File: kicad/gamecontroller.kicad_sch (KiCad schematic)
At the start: 19 parts, among them SW1 SW_Push, SW2 SW_Push, SW3 SW_Push, SW4 SW_Push, SW5 SW_Push, SW6 SW_Push

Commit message: Updates to kicad files and update espinput submodule
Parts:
- removed U1: ~, ESP32_30pin:ESP32_30pin, symbol esp32_30pin:ESP32_30Pin
- added COM-09302: COM-09032, COM_09032:COM_09032, symbol COM-09032:COM-09032
- added D1: LED, LED_THT:LED_D3.0mm, symbol Device:LED
- added ESP32: ESP32_30pin, ESP32_30pin:ESP32_30pin, symbol ESP32_30pin:ESP32_30Pin
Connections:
- net +3.3V: now also COM-09302.H1 (H+), COM-09302.V1 (V+)
- net GND: now also COM-09302.B2A (SEL-), COM-09302.H3 (H-), COM-09302.V3 (V-)
- no-connect marks 24 -> 28

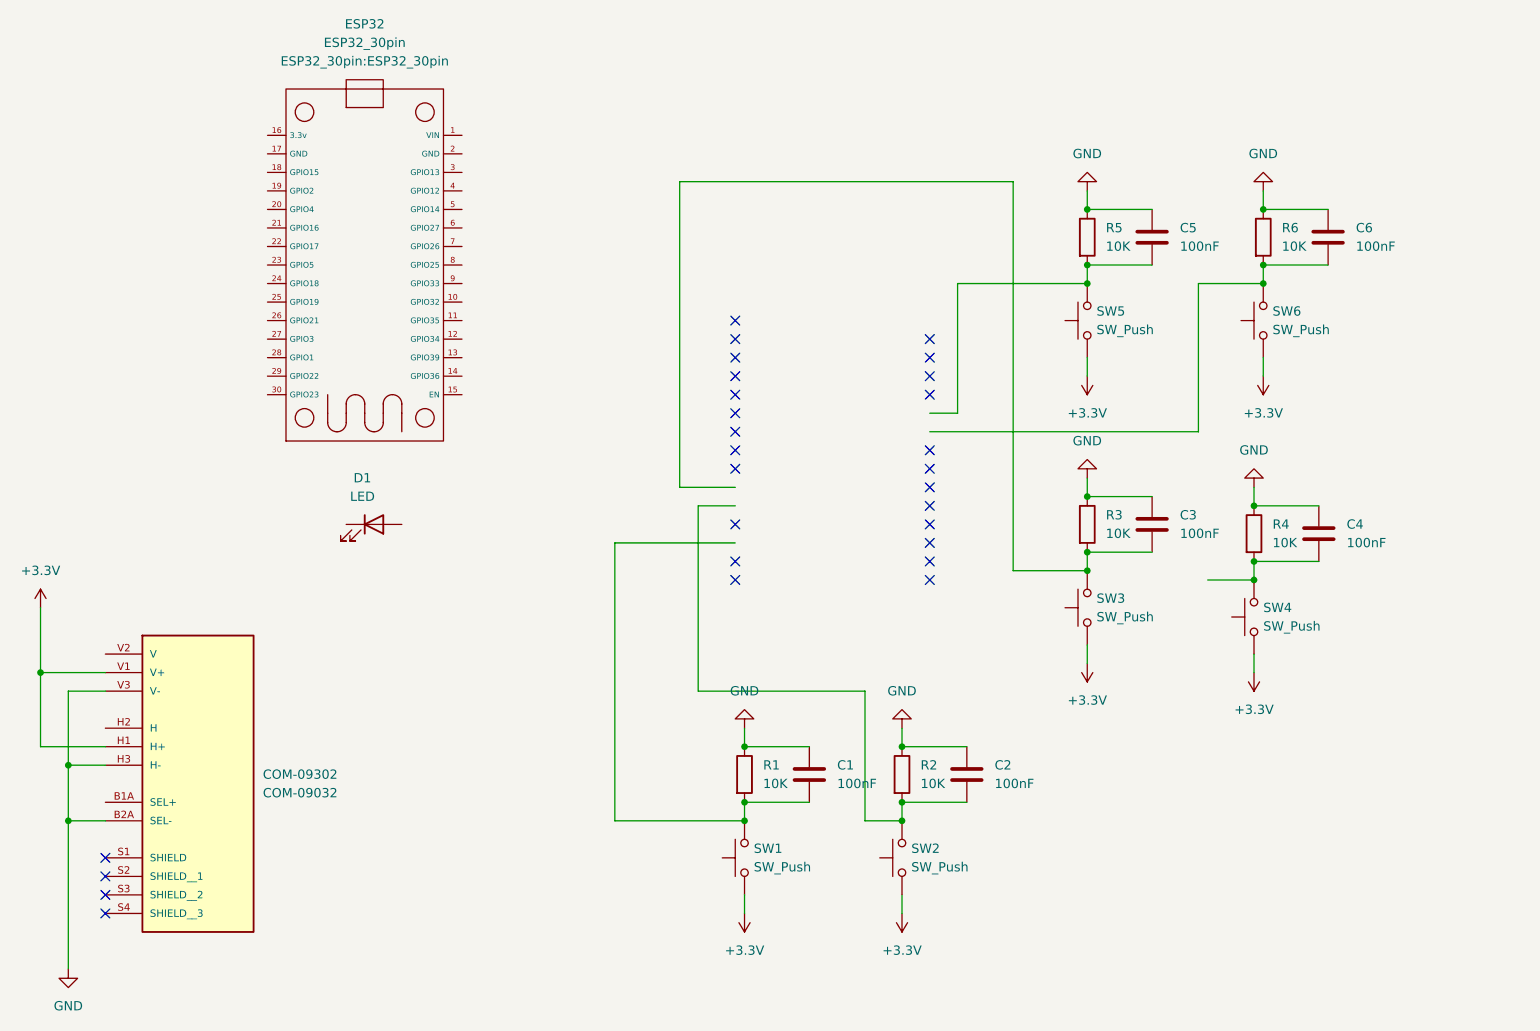
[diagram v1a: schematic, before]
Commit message: Update kicad, gerber, and spice files
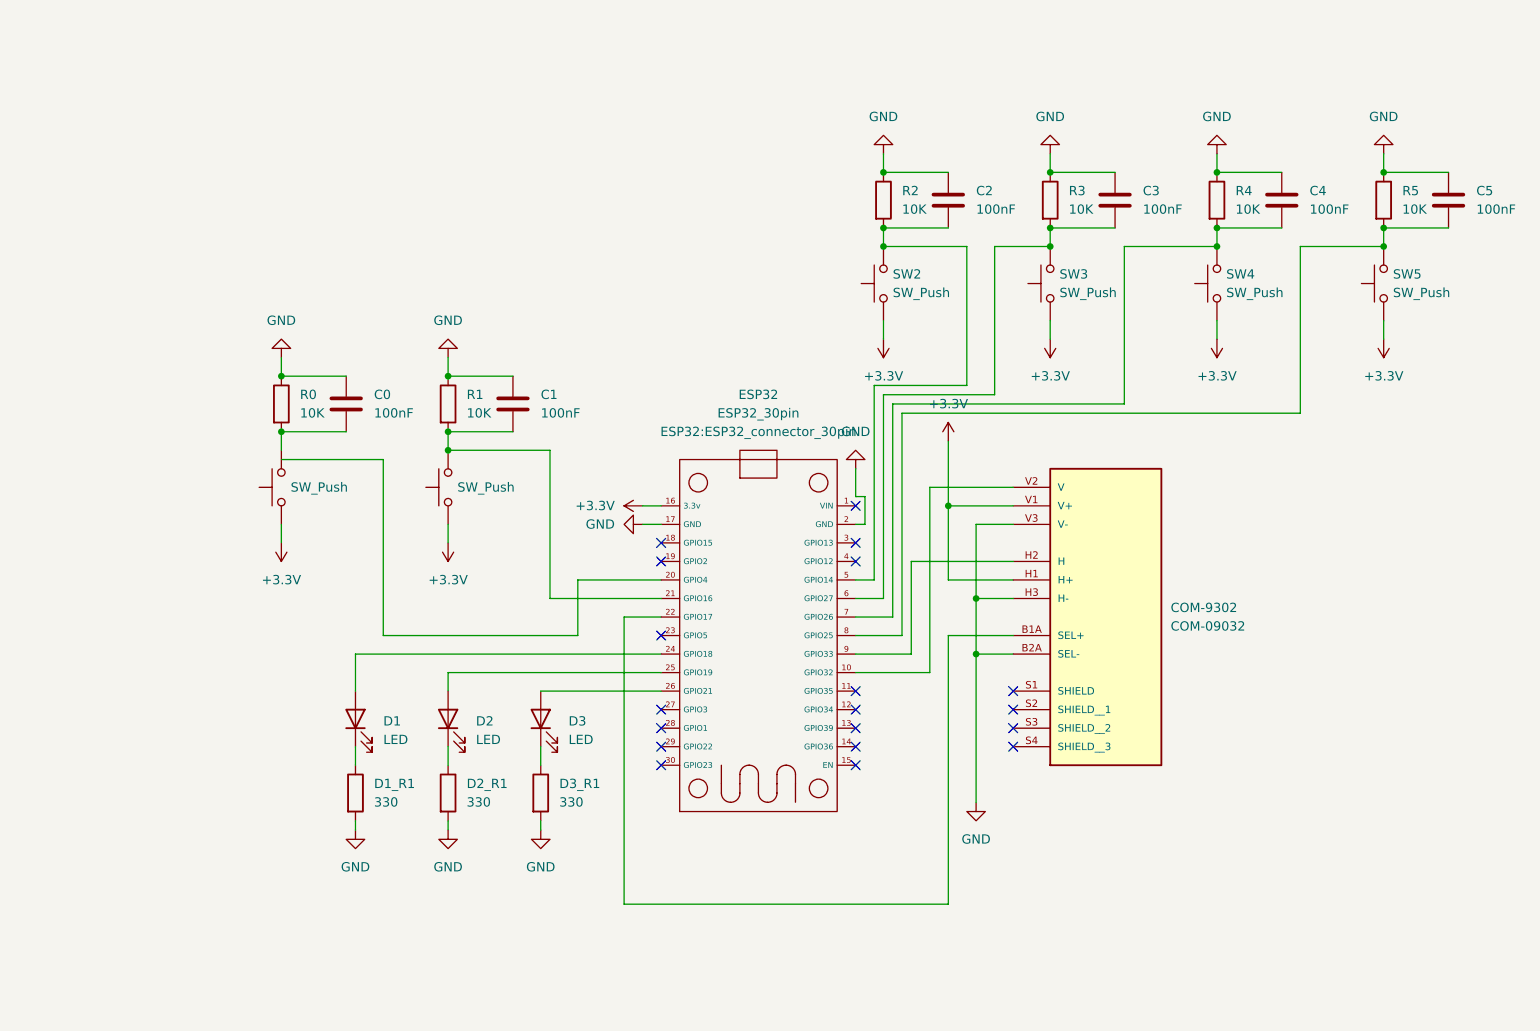
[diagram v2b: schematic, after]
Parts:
- removed COM-09302: COM-09032, COM_09032:COM_09032, symbol COM-09032:COM-09032
- added COM-9302: COM-09032, COM_09302:XDCR_COM-09032, symbol COM_09302:COM-09032
- added D1_R1, D2_R1, D3_R1: 330, Resistor_THT:R_Axial_DIN0207_L6.3mm_D2.5mm_P7.62mm_Horizontal, symbol Device:R
- added D2, D3: LED, LED_THT:LED_D3.0mm, symbol Device:LED
- ESP32: footprint ESP32_30pin:ESP32_30pin -> ESP32:ESP32_connector_30pin
- R0: renamed from R6; footprint Resistor_THT:R_Axial_DIN0207_L6.3mm_D2.5mm_P5.08mm_Vertical -> Resistor_THT:R_Axial_DIN0207_L6.3mm_D2.5mm_P7.62mm_Horizontal
- R1, R2, R3, R4, R5: footprint Resistor_THT:R_Axial_DIN0207_L6.3mm_D2.5mm_P5.08mm_Vertical -> Resistor_THT:R_Axial_DIN0207_L6.3mm_D2.5mm_P7.62mm_Horizontal
- SW0: renamed from SW6; footprint Button_Switch_THT:SW_PUSH-12mm -> Button_Switch_THT:SW_PUSH_6mm
- SW1: footprint Button_Switch_THT:SW_PUSH-12mm -> Button_Switch_THT:SW_PUSH_6mm
- renumbered C6 to C0
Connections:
- net +3.3V: now also ESP32.16 (3.3v), COM-9302.H1 (H+), COM-9302.V1 (V+)
- net GND: now also ESP32.17 (GND), ESP32.2 (GND), COM-9302.B2A (SEL-), COM-9302.H3 (H-), COM-9302.V3 (V-), D1_R1.2, D2_R1.2, D3_R1.2
- net at C5.2, R5.2, SW5.2: now also ESP32.8 (GPIO25)
- net at C3.2, R3.2, SW3.2: now also ESP32.6 (GPIO27)
- net at C2.2, R2.2, SW2.2: now also ESP32.5 (GPIO14)
- net at D1.1 (K): now also D1_R1.1
- net at D1.2 (A): now also ESP32.24 (GPIO18)
- net at C1.2, R1.2, SW1.2: now also ESP32.21 (GPIO16)
- net at ESP32.10 (GPIO32): now also COM-9302.V2 (V)
- net at ESP32.22 (GPIO17): now also COM-9302.B1A (SEL+)
- net at ESP32.25 (GPIO19): now also D2.2 (A)
- net at ESP32.26 (GPIO21): now also D3.2 (A)
- net at ESP32.7 (GPIO26): now also C4.2, R4.2, SW4.2
- net at ESP32.9 (GPIO33): now also COM-9302.H2 (H)
- new net: D3.1 (K), D3_R1.1
- new net: D2.1 (K), D2_R1.1
- no-connect marks 28 -> 19
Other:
- moved on the sheet: C0, C1, C2, C3, C4, C5, D1, ESP32, R0, R1, R2, R3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
